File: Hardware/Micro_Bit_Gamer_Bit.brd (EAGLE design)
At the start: 152.4 x 50.8 mm, 37 parts, among them J1 Pokehome, J2 Pokehome, J3 Pokehome, J4 Pokehome, J5 Pokehome, J6 Pokehome, J7 Pokehome, J8 Pokehome, U2 micro:bit

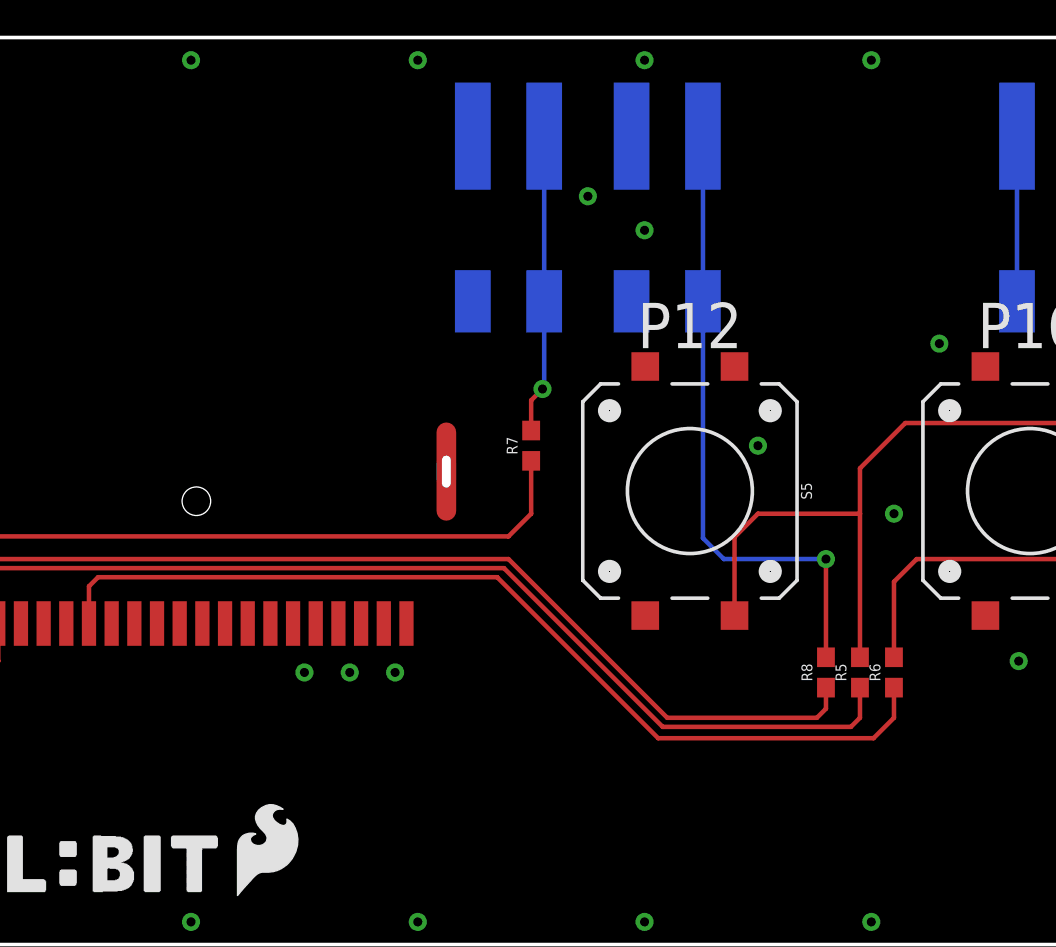
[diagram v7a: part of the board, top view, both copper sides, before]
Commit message: Added qwiic connector to back side
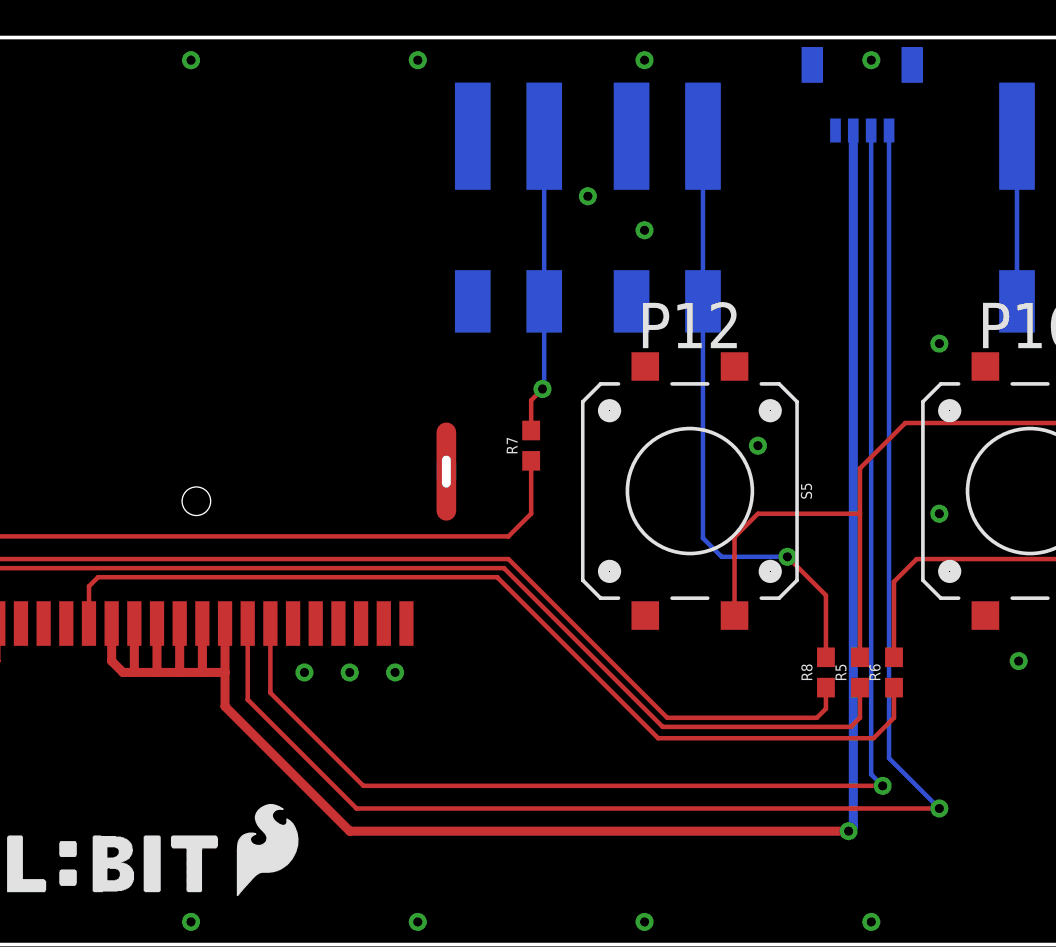
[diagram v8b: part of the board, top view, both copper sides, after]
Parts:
- added J9: QWIIC_RA, SparkFun-Connectors:JST04_1MM_RA
- added U$2: (no value), SparkFun-Aesthetics:QWIIC_5MM
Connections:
- new net SCL: J9.4, U2.P$33
- new net SDA: J9.3, U2.P$34
- net 3.3V: now also J9.2
- net GND: now also J9.1
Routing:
- net 3.3V: track 0.00 -> 101.5 mm, vias 0 -> 1
- net SCL: track 0.00 -> 84.7 mm, vias 0 -> 1
- net SDA: track 0.00 -> 77.3 mm, vias 0 -> 1
- net N$6: track 35.4 -> 34.2 mm
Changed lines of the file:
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@@
 <element name="U$4" library="Micro_Bit_Parts" package="LOGO-CONTROLBIT" value="LOGO-CONTROLBIT" x="58.95975" y="2.8575" smashed="yes"/>
 <element name="U$5" library="Micro_Bit_Parts" package="LOGO-CONTROLBIT" value="LOGO-CONTROLBIT" x="91.97975" y="30.4165" smashed="yes" rot="MR0"/>
+<element name="J9" library="SparkFun-Connectors" package="JST04_1MM_RA" value="QWIIC_RA" x="126.492" y="45.593" smashed="yes" rot="MR180">
+<attribute name="NAME" x="126.508" y="41.02666875" size="0.6096" layer="26" rot="MR180"/>
+<attribute name="PROD_ID" value="CONN-13694" x="118.872" y="36.703" size="1.778" layer="28" rot="MR180" display="off"/>
+<attribute name="VALUE" value="QWIIC_RIGHT_ANGLE" x="126.508" y="46.88933125" size="0.6096" layer="28" rot="MR180"/>
+</element>
+<element name="U$2" library="SparkFun-Aesthetics" package="QWIIC_5MM" value="" x="126.7714" y="43.6372" smashed="yes" rot="MR0"/>
 </elements>
 <signals>
@@
 <contactref element="U2" pad="P$31"/>
 <contactref element="U2" pad="P$30"/>
-<wire x1="89.535" y1="17.98" x2="90.805" y2="17.98" width="0" layer="19" extent="1-1"/>
-<wire x1="88.265" y1="17.98" x2="89.535" y2="17.98" width="0" layer="19" extent="1-1"/>
-<wire x1="86.995" y1="17.98" x2="88.265" y2="17.98" width="0" layer="19" extent="1-1"/>
-<wire x1="85.725" y1="17.98" x2="86.995" y2="17.98" width="0" layer="19" extent="1-1"/>
-<wire x1="84.455" y1="17.98" x2="85.725" y2="17.98" width="0" layer="19" extent="1-1"/>
+<contactref element="J9" pad="2"/>
+<wire x1="90.805" y1="17.98" x2="90.805" y2="15.24" width="0.508" layer="1"/>
+<wire x1="90.805" y1="15.24" x2="90.805" y2="13.335" width="0.508" layer="1"/>
+<wire x1="97.79" y1="6.35" x2="125.73" y2="6.35" width="0.508" layer="1"/>
+<via x="125.73" y="6.35" extent="1-16" drill="0.508"/>
+<wire x1="125.73" y1="6.35" x2="125.992" y2="6.612" width="0.508" layer="16"/>
+<wire x1="125.992" y1="6.612" x2="125.992" y2="45.593" width="0.508" layer="16"/>
+<wire x1="90.805" y1="13.335" x2="97.79" y2="6.35" width="0.508" layer="1"/>
+<wire x1="84.455" y1="17.98" x2="84.455" y2="15.875" width="0.508" layer="1"/>
+<wire x1="84.455" y1="15.875" x2="85.09" y2="15.24" width="0.508" layer="1"/>
+<wire x1="85.09" y1="15.24" x2="85.725" y2="15.24" width="0.508" layer="1"/>
+<wire x1="85.725" y1="15.24" x2="86.995" y2="15.24" width="0.508" layer="1"/>
+<wire x1="86.995" y1="15.24" x2="88.265" y2="15.24" width="0.508" layer="1"/>
+<wire x1="88.265" y1="15.24" x2="89.535" y2="15.24" width="0.508" layer="1"/>
+<wire x1="89.535" y1="15.24" x2="90.805" y2="15.24" width="0.508" layer="1"/>
+<wire x1="85.725" y1="17.98" x2="85.725" y2="15.24" width="0.508" layer="1"/>
+<wire x1="86.995" y1="17.98" x2="86.995" y2="15.24" width="0.508" layer="1"/>
+<wire x1="88.265" y1="17.98" x2="88.265" y2="15.24" width="0.508" layer="1"/>
+<wire x1="89.535" y1="17.98" x2="89.535" y2="15.24" width="0.508" layer="1"/>
 </signal>
 <signal name="GND">
@@
 <via x="10.795" y="43.18" extent="1-16" drill="0.508"/>
 <contactref element="S3" pad="3"/>
-<via x="128.27" y="24.13" extent="1-16" drill="0.508"/>
+<via x="130.81" y="24.13" extent="1-16" drill="0.508"/>
 <contactref element="U2" pad="P$36"/>
 <contactref element="U2" pad="P$37"/>
@@
 <via x="59.69" y="12.7" extent="1-16" drill="0.508"/>
 <via x="66.04" y="12.7" extent="1-16" drill="0.508"/>
+<contactref element="J9" pad="1"/>
 </signal>
 <signal name="N$1">
@@
 <contactref element="J8" pad="P2"/>
 <wire x1="117.57" y1="36.025" x2="117.57" y2="45.275" width="0.254" layer="16"/>
-<via x="124.46" y="21.59" extent="1-16" drill="0.508"/>
+<via x="122.301" y="21.717" extent="1-16" drill="0.508"/>
 <wire x1="117.57" y1="36.025" x2="117.57" y2="22.765" width="0.254" layer="16"/>
-<wire x1="124.46" y1="16.09" x2="124.46" y2="21.59" width="0.254" layer="1"/>
-<wire x1="117.57" y1="22.765" x2="118.745" y2="21.59" width="0.254" layer="16"/>
-<wire x1="118.745" y1="21.59" x2="124.46" y2="21.59" width="0.254" layer="16"/>
+<wire x1="124.46" y1="16.09" x2="124.46" y2="19.558" width="0.254" layer="1"/>
+<wire x1="124.46" y1="19.558" x2="122.301" y2="21.717" width="0.254" layer="1"/>
+<wire x1="117.57" y1="22.765" x2="118.618" y2="21.717" width="0.254" layer="16"/>
+<wire x1="118.618" y1="21.717" x2="122.301" y2="21.717" width="0.254" layer="16"/>
+</signal>
+<signal name="SDA">
+<contactref element="J9" pad="3"/>
+<contactref element="U2" pad="P$34"/>
+<wire x1="126.992" y1="45.593" x2="126.992" y2="9.533" width="0.254" layer="16"/>
+<wire x1="126.992" y1="9.533" x2="127.635" y2="8.89" width="0.254" layer="16"/>
+<via x="127.635" y="8.89" extent="1-16" drill="0.508"/>
+<wire x1="127.635" y1="8.89" x2="98.552" y2="8.89" width="0.254" layer="1"/>
+<wire x1="93.345" y1="14.097" x2="93.345" y2="17.98" width="0.254" layer="1"/>
+<wire x1="98.552" y1="8.89" x2="93.345" y2="14.097" width="0.254" layer="1"/>
+</signal>
+<signal name="SCL">
+<contactref element="J9" pad="4"/>
+<contactref element="U2" pad="P$33"/>
+<wire x1="92.075" y1="17.98" x2="92.075" y2="13.716" width="0.254" layer="1"/>
+<wire x1="98.171" y1="7.62" x2="130.81" y2="7.62" width="0.254" layer="1"/>
+<via x="130.81" y="7.62" extent="1-16" drill="0.508"/>
+<wire x1="130.81" y1="7.62" x2="127.992" y2="10.438" width="0.254" layer="16"/>
+<wire x1="127.992" y1="10.438" x2="127.992" y2="45.593" width="0.254" layer="16"/>
+<wire x1="92.075" y1="13.716" x2="98.171" y2="7.62" width="0.254" layer="1"/>
 </signal>
 </signals>
